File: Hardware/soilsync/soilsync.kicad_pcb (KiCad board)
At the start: 2 copper layers, 2 parts, among them U1 STM32F103C8Tx, U2 LM2596

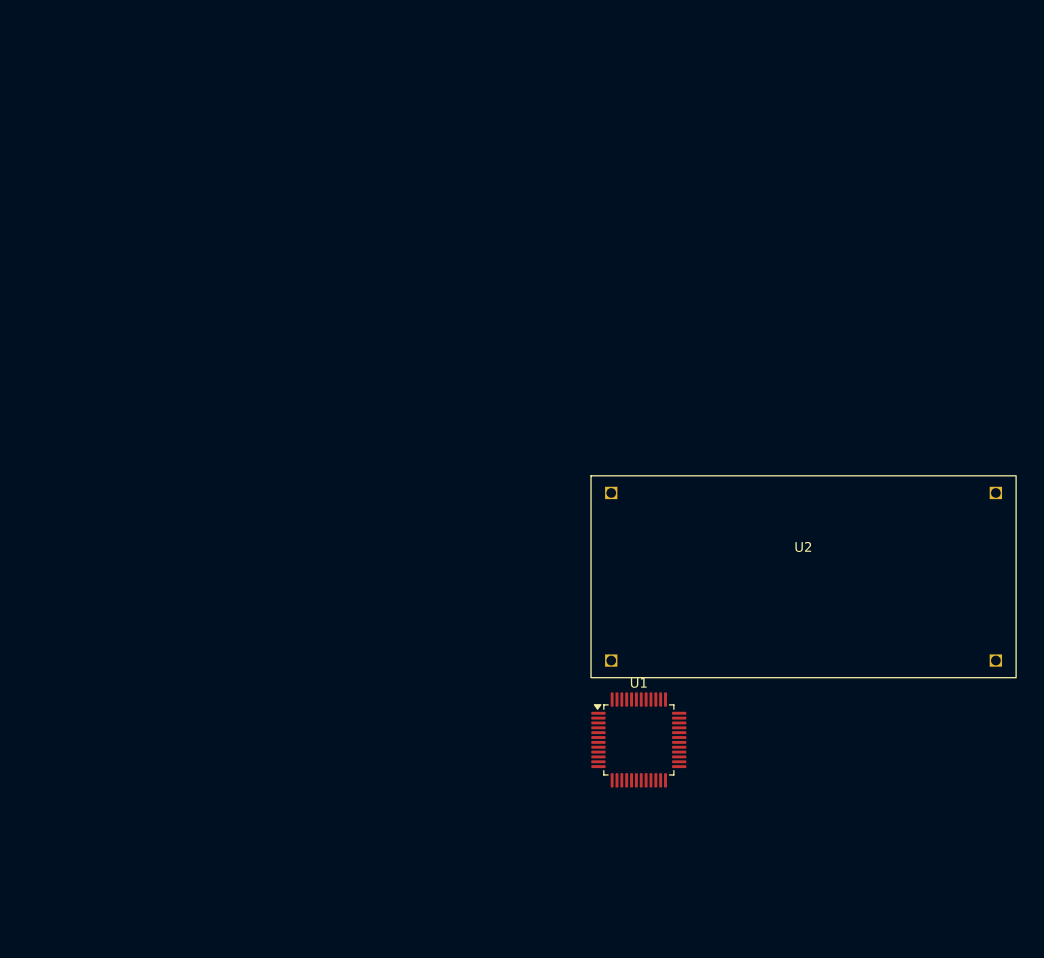
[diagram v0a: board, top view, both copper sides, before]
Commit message: updated in kicad
added custom components
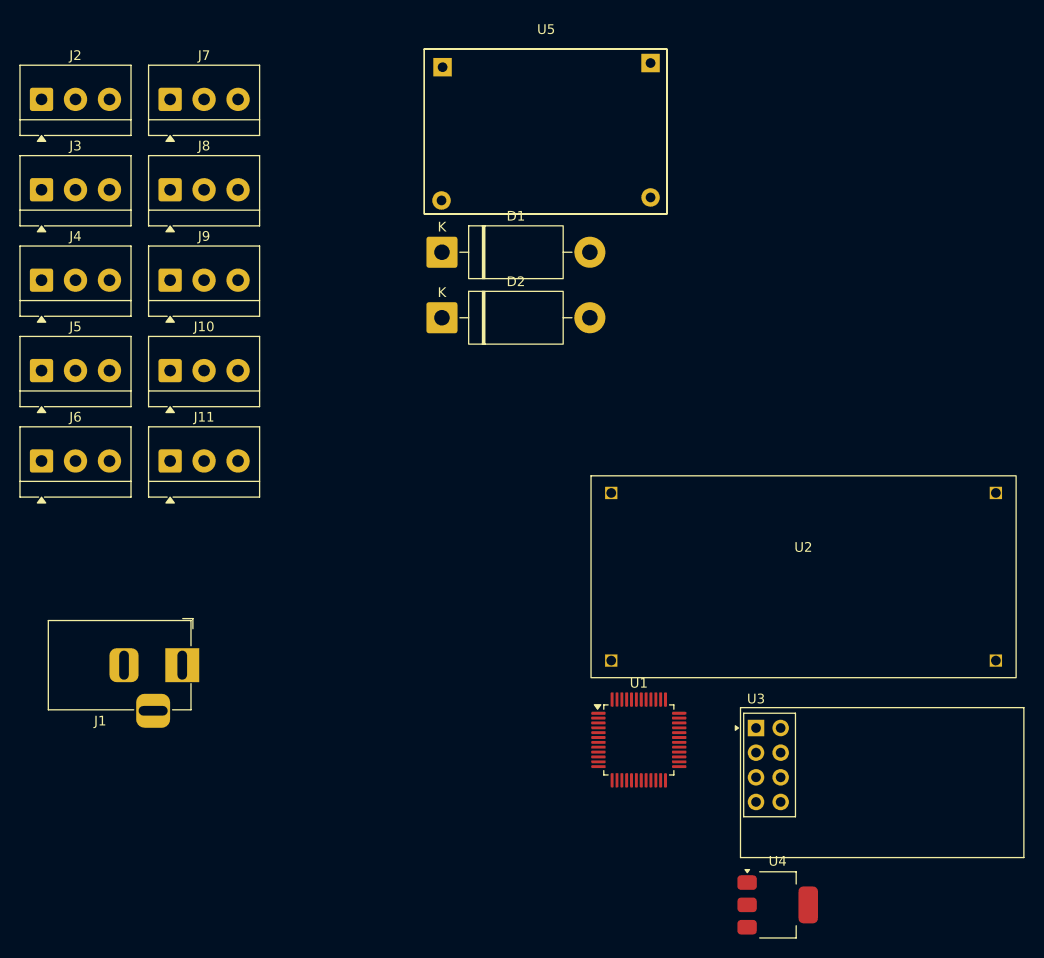
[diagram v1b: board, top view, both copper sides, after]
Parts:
- added D1: MBR340, Diode_THT:D_DO-201AD_P15.24mm_Horizontal, F.Cu at (63.8, 39.2)
- added D2: MBR340, Diode_THT:D_DO-201AD_P15.24mm_Horizontal, F.Cu at (63.8, 46.0)
- added J1: Barrel_Jack_Switch, Connector_BarrelJack:BarrelJack_Horizontal, F.Cu at (37.0, 81.8)
- added J10: Screw_Terminal_01x03, TerminalBlock_4Ucon:TerminalBlock_4Ucon_1x03_P3.50mm_Horizontal, F.Cu at (35.8, 51.4)
- added J11: Screw_Terminal_01x03, TerminalBlock_4Ucon:TerminalBlock_4Ucon_1x03_P3.50mm_Horizontal, F.Cu at (35.8, 60.8)
- added J2: Screw_Terminal_01x03, TerminalBlock_4Ucon:TerminalBlock_4Ucon_1x03_P3.50mm_Horizontal, F.Cu at (22.5, 23.5)
- added J3: Screw_Terminal_01x03, TerminalBlock_4Ucon:TerminalBlock_4Ucon_1x03_P3.50mm_Horizontal, F.Cu at (22.5, 32.8)
- added J4: Screw_Terminal_01x03, TerminalBlock_4Ucon:TerminalBlock_4Ucon_1x03_P3.50mm_Horizontal, F.Cu at (22.5, 42.1)
- added J5: Screw_Terminal_01x03, TerminalBlock_4Ucon:TerminalBlock_4Ucon_1x03_P3.50mm_Horizontal, F.Cu at (22.5, 51.4)
- added J6: Screw_Terminal_01x03, TerminalBlock_4Ucon:TerminalBlock_4Ucon_1x03_P3.50mm_Horizontal, F.Cu at (22.5, 60.8)
- added J7: Screw_Terminal_01x03, TerminalBlock_4Ucon:TerminalBlock_4Ucon_1x03_P3.50mm_Horizontal, F.Cu at (35.8, 23.5)
- added J8: Screw_Terminal_01x03, TerminalBlock_4Ucon:TerminalBlock_4Ucon_1x03_P3.50mm_Horizontal, F.Cu at (35.8, 32.8)
- added J9: Screw_Terminal_01x03, TerminalBlock_4Ucon:TerminalBlock_4Ucon_1x03_P3.50mm_Horizontal, F.Cu at (35.8, 42.1)
- added U3: NRF24L01_Breakout, RF_Module:nRF24L01_Breakout, F.Cu at (96.1, 88.3)
- added U4: AMS1117-3.3, Package_TO_SOT_SMD:SOT-223-3_TabPin2, F.Cu at (98.3, 106.5)
- added U5: TP5100, Modules:TP5100_Module, F.Cu at (74.4, 26.8)
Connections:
- U1 pad 10: unconnected-(U1-PA0-Pad10) -> SENSOR_1
- U1 pad 11: unconnected-(U1-PA1-Pad11) -> SENSOR_2
- U1 pad 12: unconnected-(U1-PA2-Pad12) -> SENSOR_3
- U1 pad 13: unconnected-(U1-PA3-Pad13) -> SENSOR_4
- U1 pad 14: unconnected-(U1-PA4-Pad14) -> SENSOR_5
- U1 pad 15: unconnected-(U1-PA5-Pad15) -> SENSOR_6
- U1 pad 16: unconnected-(U1-PA6-Pad16) -> SENSOR_7
- U1 pad 17: unconnected-(U1-PA7-Pad17) -> SENSOR_8
- U1 pad 18: unconnected-(U1-PB0-Pad18) -> SENSOR_9
- U1 pad 19: unconnected-(U1-PB1-Pad19) -> SENSOR_10
- U1 pad 25: unconnected-(U1-PB12-Pad25) -> /NRF_CSN
- U1 pad 26: unconnected-(U1-PB13-Pad26) -> /NRF_SCK
- U1 pad 27: unconnected-(U1-PB14-Pad27) -> /NRF_MISO
- U1 pad 28: unconnected-(U1-PB15-Pad28) -> /NRF_MISO
- U1 pad 29: unconnected-(U1-PA8-Pad29) -> /NRF_CE
- U1 pad 40: unconnected-(U1-PB4-Pad40) -> /PUMP
- U2 pad 1: unconnected-(U2-IN+-Pad1) -> /VIN
- U2 pad 2: unconnected-(U2-IN--Pad2) -> GND
- U2 pad 3: unconnected-(U2-OUT+-Pad3) -> +5V
- U2 pad 4: unconnected-(U2-OUT--Pad4) -> GND

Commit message: a little changes in footprints
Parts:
- U1: footprint Package_QFP:LQFP-48_7x7mm_P0.5mm -> Package_DIP:DIP-40_W15.24mm_LongPads
- moved J7 236.4 mm to (256.5, 108.0), turned to 90 degrees
- moved J8 228.9 mm to (256.5, 93.2), turned to 90 degrees
- moved J9 223.8 mm to (256.5, 78.5), turned to 90 degrees
- moved J10 221.1 mm to (256.5, 63.7), turned to 90 degrees
- moved J11 221.1 mm to (256.5, 49.0), turned to 90 degrees
- moved J1 157.5 mm to (191.8, 110.8), turned to 90 degrees
- moved J6 155.5 mm to (172.7, 100.9), turned to -90 degrees
- moved J5 154.2 mm to (172.7, 86.1), turned to -90 degrees
- moved J4 153.0 mm to (172.7, 71.4), turned to -90 degrees
- moved J3 152.1 mm to (172.7, 56.6), turned to -90 degrees
- moved J2 151.3 mm to (172.7, 41.9), turned to -90 degrees
- moved D1 137.3 mm to (191.8, 88.9), turned to -90 degrees
- moved U1 137.0 mm to (221.0, 92.7), turned to 180 degrees
- moved U3 109.5 mm to (190.0, 31.8), turned to 90 degrees
- moved U5 36.2 mm to (109.2, 36.8)
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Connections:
- D1 pad 1: unconnected-(D1-K-Pad1) -> VIN
- D1 pad 2: unconnected-(D1-A-Pad2) -> Net-(D1-A)
- J1 pad 1: unconnected-(J1-Pad1) -> Net-(D1-A)
- J1 pad 2: unconnected-(J1-Pad2) -> GND
- U2 pad 1: /VIN -> VIN

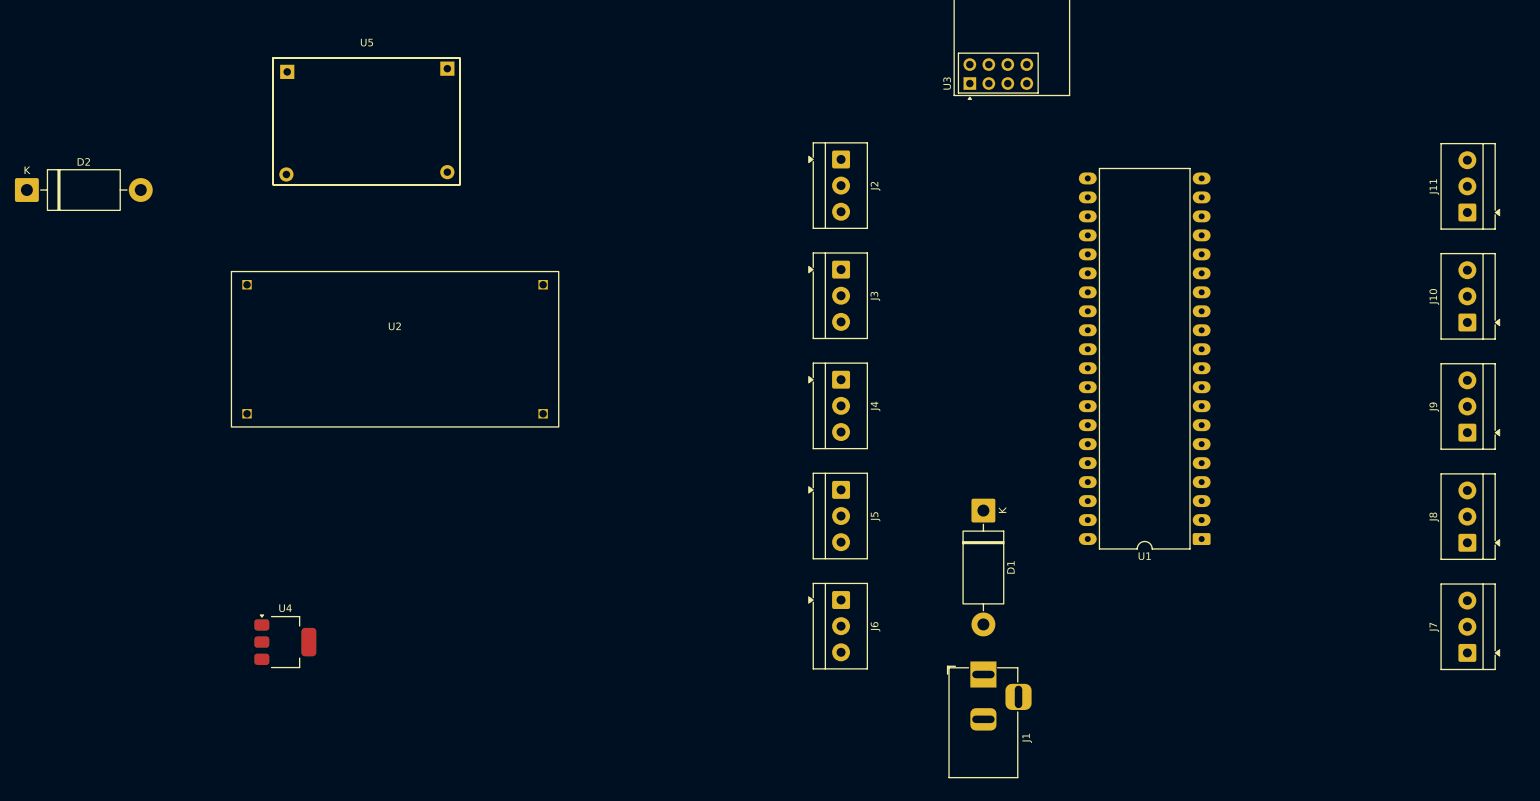
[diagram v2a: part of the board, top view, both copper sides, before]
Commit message: major PCB updates
placement & routing
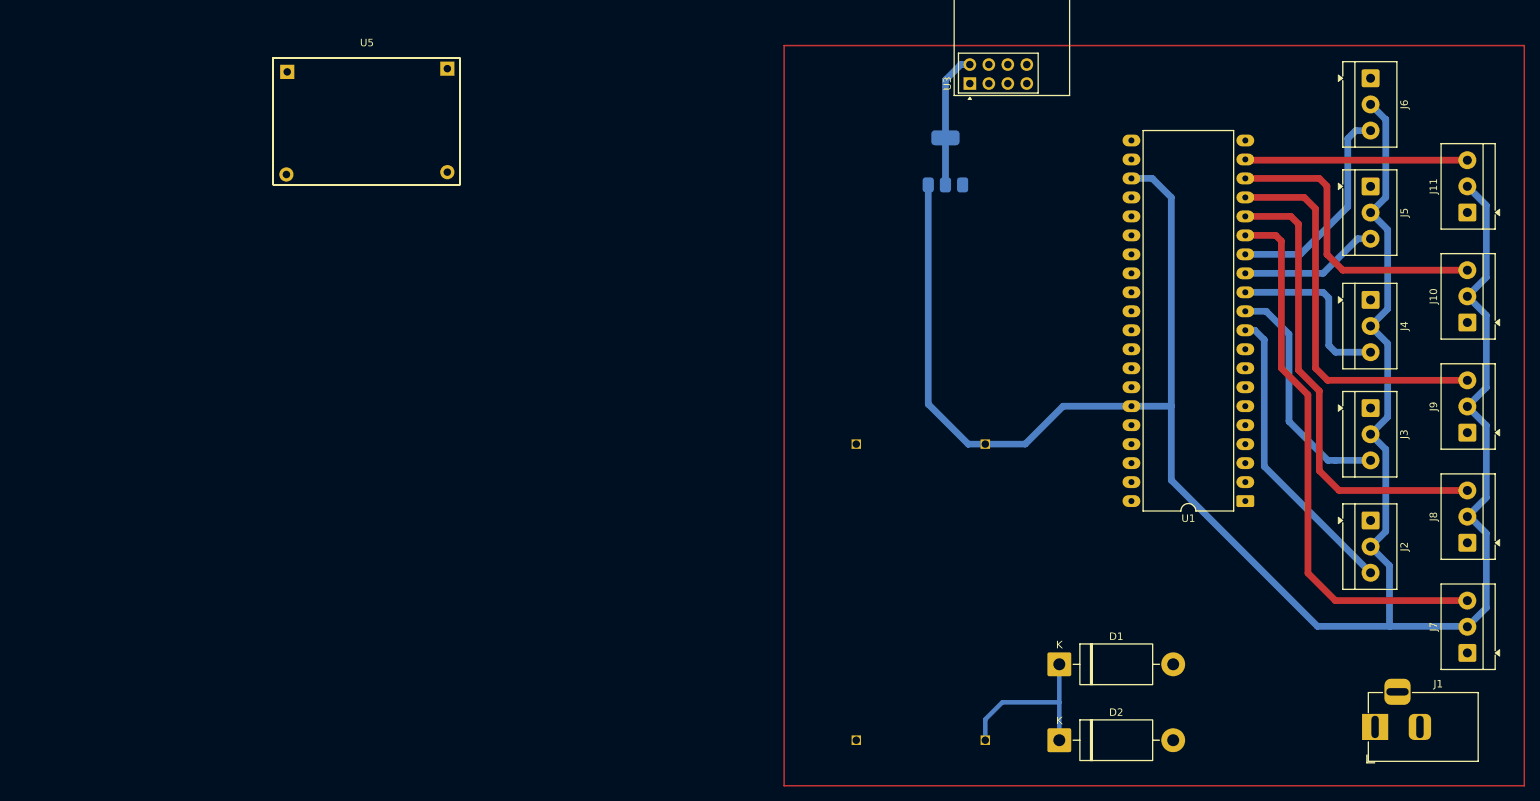
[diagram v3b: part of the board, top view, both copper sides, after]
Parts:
- U2, U4: moved to B.Cu
- moved D2 156.6 mm to (201.9, 119.6)
- moved U2 121.4 mm to (193.8, 121.7), turned to 90 degrees
- moved U4 109.3 mm to (186.7, 42.2), turned to 90 degrees
- moved J6 99.5 mm to (243.6, 31.0)
- moved J2 85.8 mm to (243.6, 90.2)
- moved J5 81.7 mm to (243.6, 45.5)
- moved J3 73.2 mm to (243.6, 75.2)
- moved J4 71.7 mm to (243.6, 60.7)
- moved J1 52.9 mm to (244.2, 117.9), turned to 180 degrees
- moved D1 22.9 mm to (201.9, 109.5), turned to 0 degrees
- moved U1 7.74 mm to (226.8, 87.6)
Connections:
- D2 pad 1: unconnected-(D2-K-Pad1) -> VIN
- D2 pad 2: unconnected-(D2-A-Pad2) -> Net-(D2-A)
- U1 pad 23: Net-(U1-VSS-Pad23) -> +5V
- U1 pad 35: Net-(U1-VSS-Pad23) -> +5V
- U5 pad 1: unconnected-(U5-BAT+-Pad1) -> /BAT+
- U5 pad 2: unconnected-(U5-BAT--Pad2) -> /BAT-
- U5 pad 3: unconnected-(U5-VCC-Pad3) -> Net-(D2-A)
- U5 pad 4: unconnected-(U5-GND-Pad4) -> GND
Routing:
- net +5V: track 0.00 -> 303.8 mm
- net SENSOR_6: track 0.00 -> 73.9 mm
- net SENSOR_7: track 0.00 -> 62.6 mm
- net SENSOR_8: track 0.00 -> 52.4 mm
- net SENSOR_9: track 0.00 -> 40.2 mm
- net SENSOR_1: track 0.00 -> 40.1 mm
- net SENSOR_2: track 0.00 -> 31.9 mm
- net SENSOR_10: track 0.00 -> 29.8 mm
- net SENSOR_5: track 0.00 -> 29.0 mm
- net VIN: track 0.00 -> 23.8 mm
- net SENSOR_3: track 0.00 -> 23.8 mm
- net SENSOR_4: track 0.00 -> 18.7 mm
- net +3.3V: track 0.00 -> 18.2 mm
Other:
- board text added: "${REFERENCE}"

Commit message: Layout adjustments
tbf
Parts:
- added J12: Screw_Terminal_01x03, TerminalBlock_4Ucon:TerminalBlock_4Ucon_1x03_P3.50mm_Horizontal, F.Cu at (233.9, 119.1)
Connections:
- U1 pad 40: /PUMP -> PUMP
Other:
- board text added: "SENSOR_1"
- board text added: "SENSOR_10"
- board text added: "SENSOR_2"
- board text added: "SENSOR_3"
- board text added: "SENSOR_4"
- board text added: "SENSOR_5"
- board text added: "SENSOR_6"
- board text added: "SENSOR_7"
- board text added: "SENSOR_8"
- board text added: "SENSOR_9"

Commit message: finishing PCB
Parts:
- added J13: Conn_Battery, TerminalBlock_4Ucon:TerminalBlock_4Ucon_1x03_P3.50mm_Horizontal, F.Cu at (139.9, 135.1)
- added U6: HX-2S, CustomModule:HX-2S BMS module, F.Cu at (142.2, 98.9)
- moved U5 129.1 mm to (211.9, 115.0)
- moved D1 28.9 mm to (230.8, 109.0)
- moved D2 25.5 mm to (219.0, 100.7), turned to 180 degrees
- moved U4 11.2 mm to (181.9, 32.0)
- moved J12 8.15 mm to (241.9, 120.5)
- moved J1 4.76 mm to (248.9, 118.5)
- moved U2 4.50 mm to (189.8, 123.9)
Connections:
- D2 pad 2: Net-(D2-A) -> /BAT+
- U1 pad 28: /NRF_MISO -> /NRF_MOSI
- U5 pad 3: Net-(D2-A) -> VIN
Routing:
- net PUMP: track 0.00 -> 45.7 mm
- net /NRF_CE: track 0.00 -> 37.0 mm
- net /NRF_MOSI: track 0.00 -> 36.5 mm
- net /NRF_CSN: track 0.00 -> 35.2 mm
- net +5V: track 303.8 -> 270.1 mm
- net /NRF_MISO: track 0.00 -> 29.5 mm
- net /NRF_SCK: track 0.00 -> 28.6 mm
- net VIN: track 23.8 -> 0.00 mm
- net Net-(D1-A): track 0.00 -> 10.7 mm
- net +3.3V: track 18.2 -> 8.18 mm
- net SENSOR_6: track 73.9 -> 73.4 mm
